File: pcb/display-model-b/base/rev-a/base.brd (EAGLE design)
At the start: 121.9 x 17.8 mm, 41 parts, among them J1 SNG-2MM-HEADER-07-V, Q1 MMBT3904, Q2 MMBT3904, Q3 MMBT3904, Q4 MMBT3904, U1 PCA9634PW, U2 TSL2561FN, X1 CLOCK_LED_SEGMENT, X2 CLOCK_LED_SEGMENT, X3 CLOCK_LED_SEGMENT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

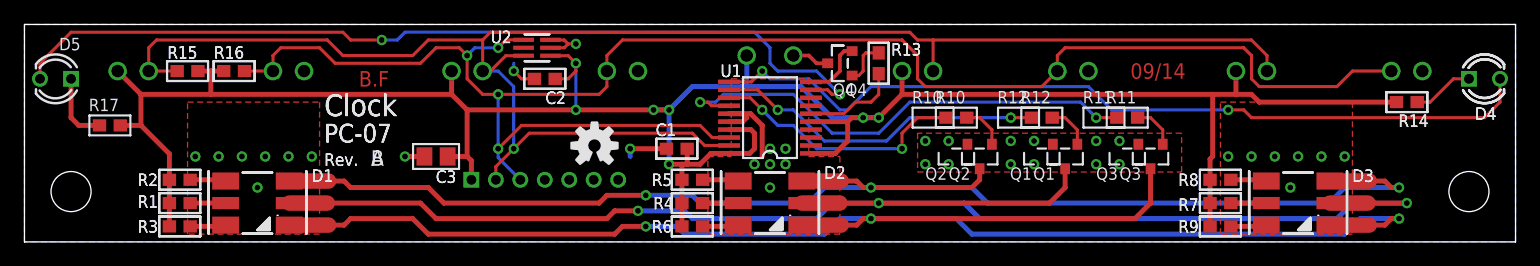
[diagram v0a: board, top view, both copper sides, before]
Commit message: Added Model B drawings
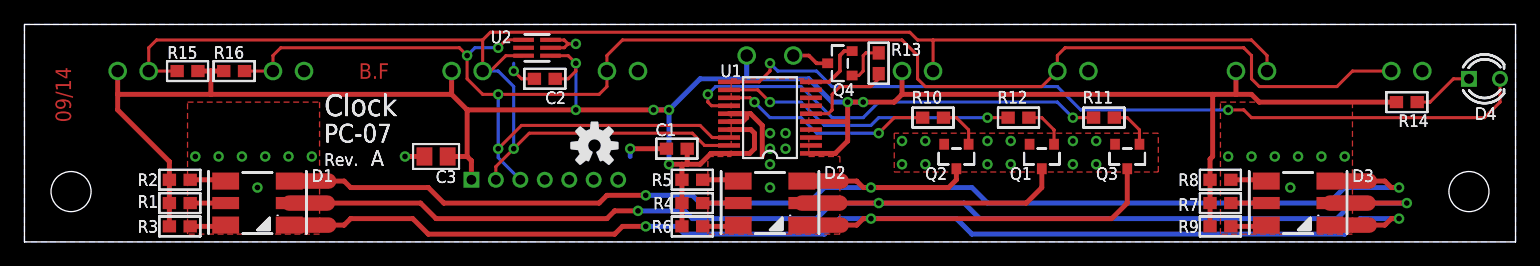
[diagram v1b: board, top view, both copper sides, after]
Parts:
- removed D5: {ATTR:COLOR}, Optoelectronic:LED_3MM
- removed R17: 82, Passive:SMD_0603
- R10, R11, R12: value 2.2k -> (none)
- R13: value 3k -> (none)
- R14: value 82 -> (none)
- moved U$1 86.7 mm to (3.81, 9.78), turned to 90 degrees
- moved Q1 1.91 mm to (83.2, 6.99)
- moved Q2 1.91 mm to (76.2, 6.99)
- moved Q3 1.91 mm to (90.2, 6.99)
- moved R10 1.91 mm to (74.3, 10.2)
- moved R11 1.91 mm to (88.3, 10.2)
- moved R12 1.91 mm to (81.3, 10.2)
- moved U$5 0.63 mm to (28.6, 14.0)
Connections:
- removed net N$20: D5.A, R17.1
- removed net N$21: D5.K, U1.9
- net 3.3V: no longer R17.2
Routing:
- net N$21: track 73.6 -> 0.00 mm, vias 2 -> 0
- net N$20: track 5.76 -> 0.00 mm
- net BL_GREEN: track 21.3 -> 17.6 mm
- net BL_BLUE: track 39.7 -> 36.4 mm
- net BL_RED: track 27.2 -> 24.3 mm
- net N$6: track 131.5 -> 129.6 mm
- net N$5: track 115.4 -> 113.5 mm
- net N$12: track 123.9 -> 122.0 mm
- net SDA: track 138.1 -> 137.0 mm
- net SCL: track 143.0 -> 142.0 mm
- net 3.3V: track 195.3 -> 194.5 mm
- net N$18: track 69.0 -> 68.3 mm
